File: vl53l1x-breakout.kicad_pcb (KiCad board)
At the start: 2 copper layers, 30 parts, among them J0 SM07B-SRSS-TBLFSN, J1 SM07B-SRSS-TBLFSN, U1 PCA9615DPJ, U2 VL53L1CXV0FY_1, U3 LTC4316IMSPBF

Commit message: [board] begin layout
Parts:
- U2: moved to B.Cu
- moved FB1 71.5 mm to (107.0, 95.8)
- moved C1 63.0 mm to (105.1, 99.9), turned to 270 degrees
- moved R6 61.8 mm to (113.3, 97.5)
- moved R4 60.3 mm to (112.9, 88.3)
- moved R2 60.1 mm to (115.5, 109.1), turned to 270 degrees
- moved R1 55.1 mm to (115.4, 105.0), turned to 270 degrees
- moved J1 53.7 mm to (237.7, 103.6)
- moved R5 48.3 mm to (113.3, 92.5)
- moved R3 47.6 mm to (115.5, 113.0), turned to 270 degrees
- moved R9 47.4 mm to (159.6, 59.9)
- moved R10 45.4 mm to (160.1, 65.3)
- moved R7 43.5 mm to (147.3, 73.7)
- moved C2 42.9 mm to (107.5, 99.9), turned to 90 degrees
- moved J0 40.1 mm to (100.5, 94.8)
- moved R8 39.1 mm to (147.5, 78.0)
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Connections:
- J0 pad 1: SDA+ -> SCL-
- J0 pad 2: SDA- -> SCL+
- J0 pad 3: SCL+ -> SDA+
- J0 pad 4: SCL- -> SDA-

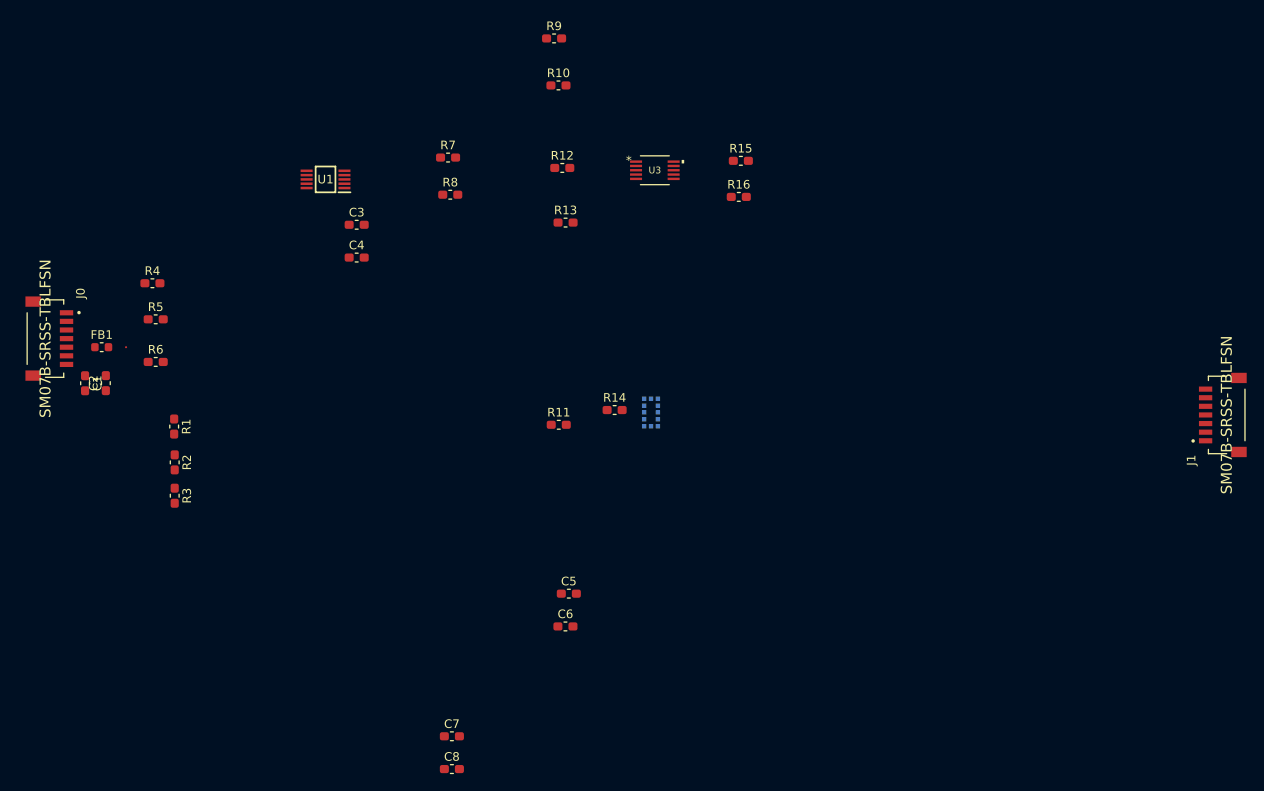
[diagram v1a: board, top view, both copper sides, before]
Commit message: [layout] smaller components; have some idea of board size
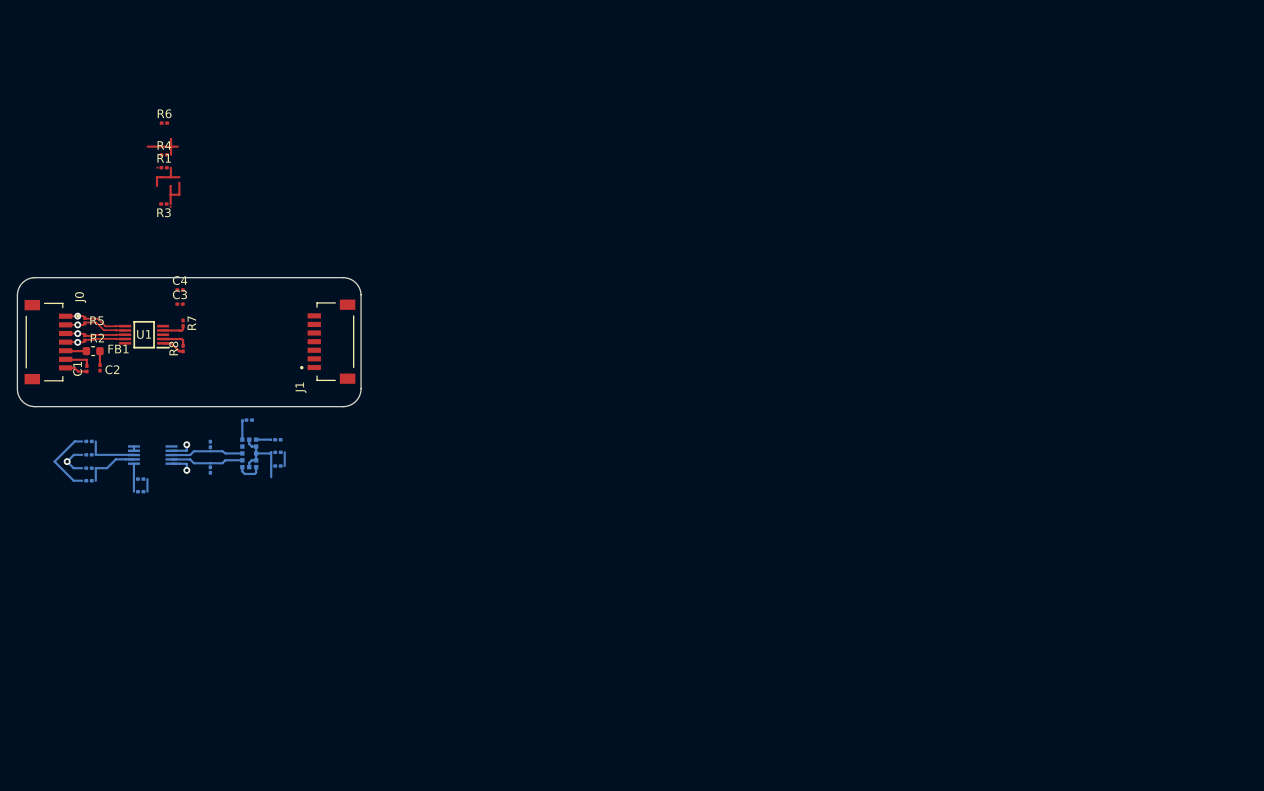
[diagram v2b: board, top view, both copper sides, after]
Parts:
- C1, C2, C3, C4: footprint Capacitor_SMD:C_0603_1608Metric_Pad1.05x0.95mm_HandSolder -> Capacitor_SMD:C_0201_0603Metric
- C5, C6, C7, C8: footprint Capacitor_SMD:C_0603_1608Metric_Pad1.05x0.95mm_HandSolder -> Capacitor_SMD:C_0201_0603Metric; moved to B.Cu
- R1, R2, R3, R4, R5, R6, R7, R8: footprint Resistor_SMD:R_0603_1608Metric_Pad1.05x0.95mm_HandSolder -> Resistor_SMD:R_0201_0603Metric
- R10, R11, R12, R13, R14, R15, R16, R9: footprint Resistor_SMD:R_0603_1608Metric_Pad1.05x0.95mm_HandSolder -> Resistor_SMD:R_0201_0603Metric; moved to B.Cu
- U3: moved to B.Cu
- moved J1 103.9 mm to (134.2, 95.1)
- moved R9 71.5 mm to (105.5, 106.7)
- moved R15 69.9 mm to (119.6, 107.1), turned to 270 degrees
- moved R10 69.4 mm to (105.5, 108.3), turned to 180 degrees
- moved R16 69.1 mm to (119.6, 110.0), turned to 90 degrees
- moved U3 67.1 mm to (113.0, 108.3)
- moved R12 65.9 mm to (105.5, 111.3)
- moved R13 62.3 mm to (105.5, 109.8), turned to 180 degrees
- moved C8 48.4 mm to (111.6, 112.5)
- moved U2 46.9 mm to (124.2, 108.1)
- moved C7 46.9 mm to (111.6, 111.1)
- moved R14 42.5 mm to (124.2, 104.2), turned to 180 degrees
- moved C6 39.1 mm to (127.5, 108.0)
- moved C5 36.9 mm to (127.5, 109.6)
- moved R7 36.3 mm to (116.5, 93.0), turned to 270 degrees
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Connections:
- C5 pad 1: Net-(C5-Pad1) -> VCC
- C6 pad 1: Net-(C5-Pad1) -> VCC
- J1 pad 4: SCL- -> SDA-
- J1 pad 5: SCL+ -> SDA+
- J1 pad 6: SDA- -> SCL+
- J1 pad 7: SDA+ -> SCL-
- R11 pad 2: Net-(C5-Pad1) -> Net-(R11-Pad2)
- U2 pad 12: Net-(C5-Pad1) -> VCC
- U2 pad 2: Net-(C5-Pad1) -> VCC
- U2 pad 3: Net-(C5-Pad1) -> VCC
- U2 pad 4: Net-(C5-Pad1) -> VCC
- U2 pad 5: Net-(C5-Pad1) -> Net-(R11-Pad2)
- U2 pad 6: Net-(C5-Pad1) -> VCC
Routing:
- net VCC: track 0.00 -> 32.7 mm, vias 0 -> 1
- net SCL+: track 0.00 -> 12.9 mm, vias 0 -> 1
- net SDA+: track 0.00 -> 12.4 mm, vias 0 -> 1
- net SDA-: track 0.00 -> 12.3 mm, vias 0 -> 1
- net Net-(R16-Pad2): track 0.00 -> 8.57 mm
- net Net-(R15-Pad2): track 0.00 -> 8.50 mm
- net SCL-: track 0.00 -> 7.56 mm, vias 0 -> 1
- net Net-(R12-Pad2): track 0.00 -> 6.32 mm
- net GND: track 0.00 -> 6.19 mm
- net Net-(R10-Pad1): track 0.00 -> 6.00 mm
- net SDA: track 0.00 -> 5.71 mm, vias 0 -> 1
- net SCL: track 0.00 -> 5.32 mm, vias 0 -> 1
- net shld: track 0.00 -> 2.65 mm
- net Net-(R14-Pad2): track 0.00 -> 2.33 mm
- net +3V3: track 0.00 -> 1.90 mm
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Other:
- board outline added: 39.9 x 15 mm

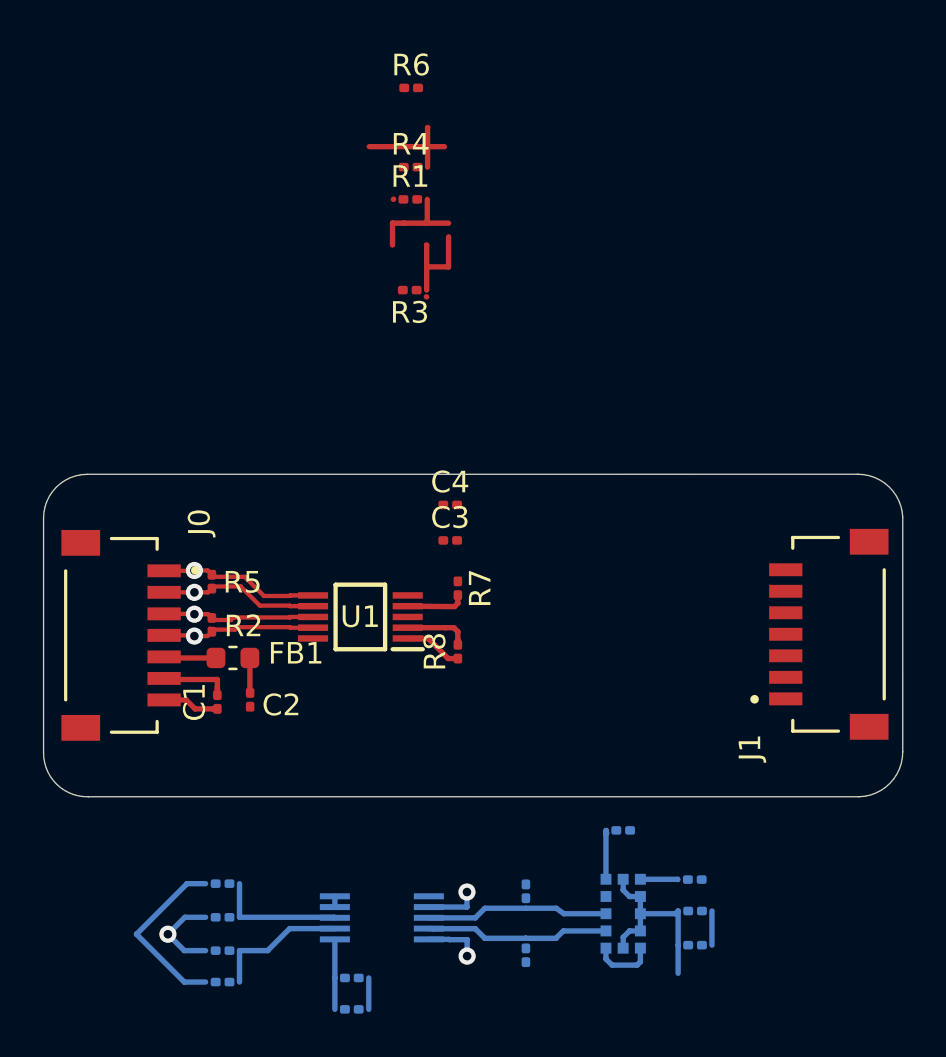
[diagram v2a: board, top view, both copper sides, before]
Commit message: [LTC4316] update footprint
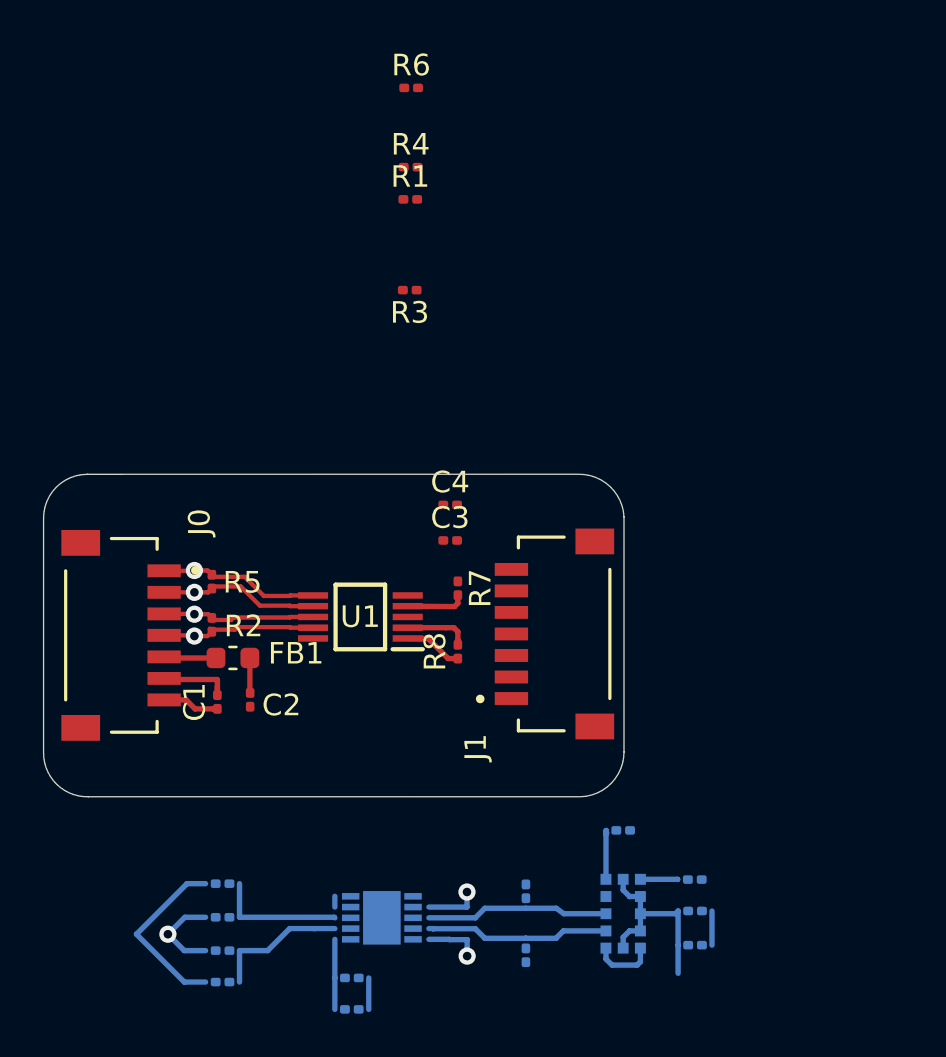
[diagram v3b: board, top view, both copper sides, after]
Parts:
- U3: footprint LTC4316:MSOP-10_MS -> LTC4316IDDPBF:DFN-10_DD
- moved J1 12.8 mm to (121.4, 95.1)
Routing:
- net SCL+: track 12.9 -> 7.55 mm
- net SDA+: track 12.4 -> 7.53 mm
- net SDA-: track 12.3 -> 7.75 mm
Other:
- board size 39.9 x 15 mm -> 27 x 15 mm

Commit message: [layout] complete overhaul
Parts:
- C5, C6, C7, C8, R11, R12, R15, R16, R9, U2, U3: moved to F.Cu
- R1, R3, R4, R6: value 600 -> 390
- R14: value 0 -> 10k; moved to F.Cu
- moved R6 61.0 mm to (111.2, 130.7), turned to 270 degrees
- moved R4 57.3 mm to (112.0, 130.7), turned to 90 degrees
- moved R1 55.8 mm to (112.8, 130.7), turned to 90 degrees
- moved R3 51.6 mm to (113.7, 130.7), turned to 270 degrees
- moved J0 40.8 mm to (129.5, 123.8), turned to 90 degrees
- moved R5 37.4 mm to (111.6, 129.5), turned to 180 degrees
- moved C4 36.8 mm to (115.3, 125.9)
- moved R2 35.8 mm to (113.3, 129.5), turned to 0 degrees
- moved C3 34.4 mm to (115.3, 125.2)
- moved J1 32.3 mm to (106.6, 123.8), turned to 270 degrees
- moved U1 31.3 mm to (112.7, 125.6), turned to 270 degrees
- moved R7 27.8 mm to (112.3, 120.5)
- moved R8 24.7 mm to (113.3, 120.5), turned to 270 degrees
- moved C1 23.5 mm to (110.7, 121.1), turned to 270 degrees
- moved FB1 22.0 mm to (112.0, 117.3)
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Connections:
- R10 pad 2: VCC -> GND
- R11 pad 1: VCC -> Net-(R11-Pad1)
- R11 pad 2: Net-(R11-Pad2) -> VCC
- R13 pad 2: VCC -> GND
- U1 pad 5: VCC -> GND
- U2 pad 12: VCC -> GND
- U2 pad 2: VCC -> GND
- U2 pad 3: VCC -> GND
- U2 pad 4: VCC -> GND
- U2 pad 5: Net-(R11-Pad2) -> Net-(R11-Pad1)
- U2 pad 6: VCC -> GND
- U3 pad 1: VCC -> GND
- U3 pad 6: VCC -> GND
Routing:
- net +3V3: track 1.90 -> 34.0 mm, vias 0 -> 2
- net SDA-: track 7.75 -> 35.6 mm, vias 1 -> 2
- net SDA+: track 7.53 -> 34.9 mm, vias 1 -> 2
- net SCL+: track 7.55 -> 34.2 mm, vias 1 -> 2
- net SCL-: track 7.56 -> 33.3 mm, vias 1 -> 2
- net VCC: track 32.6 -> 55.2 mm, vias 1 -> 6
- net shld: track 2.65 -> 24.8 mm, vias 0 -> 2
- net SCL: track 5.32 -> 18.0 mm, vias 1 -> 2
- net GND: track 6.19 -> 18.5 mm, vias 0 -> 7
- net SDA: track 5.71 -> 12.2 mm, vias 1 -> 2
- net Net-(R12-Pad2): track 6.32 -> 3.04 mm, vias 0 -> 1
- net Net-(R10-Pad1): track 6.00 -> 3.04 mm, vias 0 -> 1
- net Net-(R11-Pad1): track 0.00 -> 2.10 mm
- net Net-(R11-Pad2): track 1.75 -> 0.00 mm
- net Net-(R15-Pad2): track 8.50 -> 7.93 mm
- added copper zone on B.Cu, net GND
- added copper zone on F.Cu, net GND
- added copper zone on In2.Cu, net GND
- added copper zone on In1.Cu, net VCC
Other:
- board size 27 x 15 mm -> 28 x 21.5 mm
- copper layers 2 -> 4
- rule trace_min: 0.2 -> 0.1254
- board text added: "SHD GND 3V3 SDA- SDA+ SCL+ SCL-"
- board text added: "VL53L1X Diff. Breakout @kemfic 2022 rev. 0"

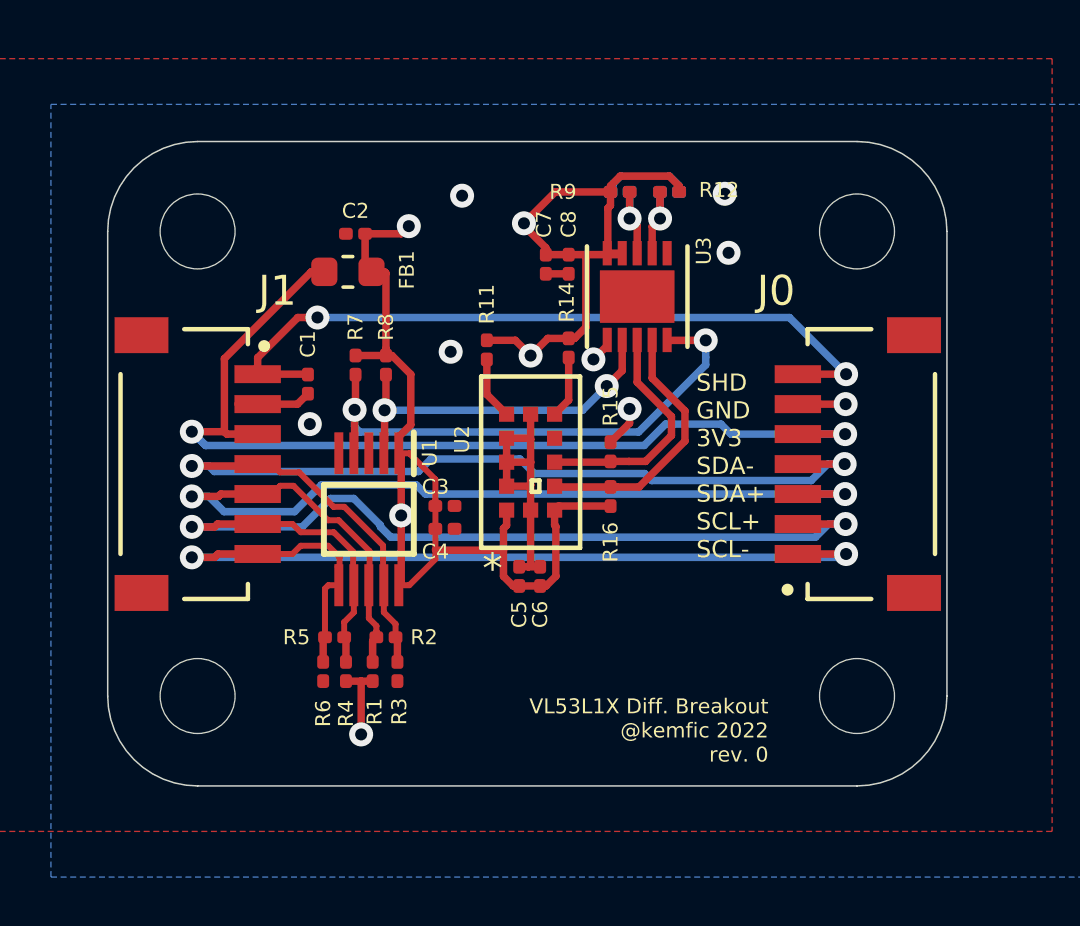
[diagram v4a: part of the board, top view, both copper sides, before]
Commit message: fixed connector pinouts
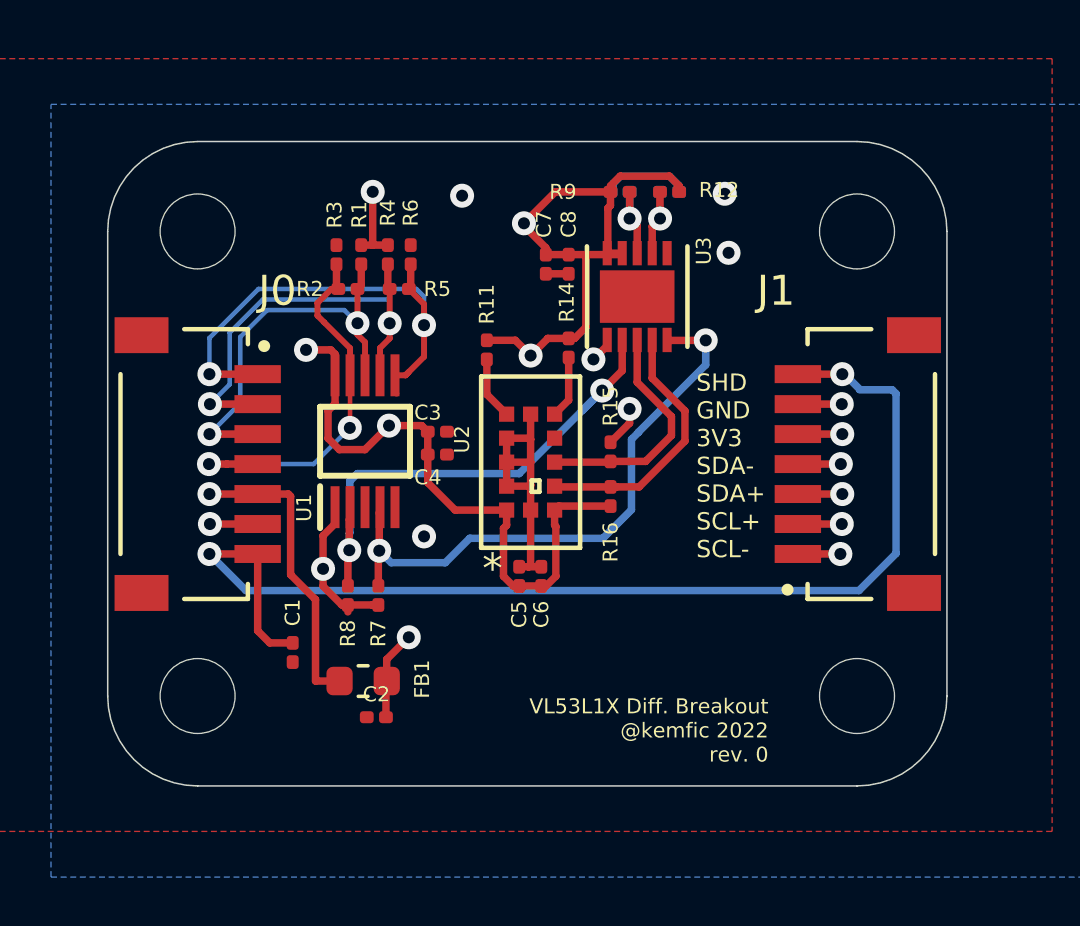
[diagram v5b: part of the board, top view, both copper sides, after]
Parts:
- moved C2 16.1 mm to (113.0, 132.2)
- moved R6 14.2 mm to (114.1, 116.8), turned to 90 degrees
- moved R3 14.1 mm to (111.6, 116.8), turned to 90 degrees
- moved R4 14.0 mm to (113.3, 116.8), turned to 270 degrees
- moved R1 13.9 mm to (112.5, 116.8), turned to 270 degrees
- moved FB1 13.7 mm to (112.5, 131.0)
- moved R5 11.8 mm to (113.7, 117.9), turned to 0 degrees
- moved R2 11.7 mm to (112.0, 117.9), turned to 180 degrees
- moved C1 8.97 mm to (110.2, 130.0)
- moved R8 7.79 mm to (112.0, 128.1), turned to 90 degrees
- moved R7 7.72 mm to (113.0, 128.1), turned to 90 degrees
- moved U1 2.61 mm to (112.6, 123.0), turned to 90 degrees
- moved C3 2.49 mm to (115.0, 122.7)
- moved C4 2.49 mm to (115.0, 123.4)
- renumbered J1 to J0, J0 to J1
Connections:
- J0 pad 1: shld -> SCL-
- J0 pad 2: GND -> SCL+
- J0 pad 3: +3V3 -> SDA+
- J0 pad 5: SDA+ -> +3V3
- J0 pad 6: SCL+ -> GND
- J0 pad 7: SCL- -> shld
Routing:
- net GND: track 18.5 -> 45.8 mm
- net shld: track 24.8 -> 38.1 mm
- net SCL-: track 33.3 -> 43.1 mm, vias 2 -> 3
- net SCL+: track 34.2 -> 41.5 mm, vias 2 -> 3
- net SDA: track 12.2 -> 17.7 mm
- net SDA-: track 35.6 -> 32.6 mm, vias 2 -> 3
- net VCC: track 55.2 -> 52.2 mm, vias 6 -> 8
- net SDA+: track 34.9 -> 37.8 mm, vias 2 -> 3
- net +3V3: track 34.0 -> 35.9 mm
- net SCL: track 18.0 -> 19.9 mm

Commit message: slightly cleaner
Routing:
- net GND: track 45.8 -> 30.3 mm, vias 7 -> 8
- net VCC: track 52.2 -> 40.8 mm, vias 8 -> 9
- net SDA-: track 32.6 -> 40.8 mm
- net shld: track 38.1 -> 32.3 mm
- net SDA+: track 37.8 -> 43.0 mm
- net +3V3: track 35.9 -> 38.4 mm
- net SCL: track 19.9 -> 18.2 mm
- net SCL+: track 41.5 -> 43.2 mm
- net SCL-: track 43.1 -> 44.7 mm
- net SDA: track 17.7 -> 16.8 mm
